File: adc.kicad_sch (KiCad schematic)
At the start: 0 parts

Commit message: Added awags and dac sheet.
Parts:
- added C47, C48: C0402_10uF_6.3V, Capacitor_SMD:C_0402_1005Metric, symbol Jojos_Lib:C0402_10uF_6.3V
- added C50, C53, C56, C59, C62: C0402_1uF_6.3V, Capacitor_SMD:C_0402_1005Metric, symbol Jojos_Lib:C0402_1uF_6.3V
- added C51, C54, C57, C60, C63: C0402_100nF_50V, Capacitor_SMD:C_0402_1005Metric, symbol Jojos_Lib:C0402_100nF_50V
- added U10, U13: 74HCT1G125GW, Package_TO_SOT_SMD:SOT-353_SC-70-5, symbol Jojos_Lib:74HCT1G125GW
- added U9: ADS8584S, Package_QFP:LQFP-64_10x10mm_P0.5mm, symbol Jojos_Lib:ADS8584S
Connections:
- new net 3.3V: C62.1, C63.1, U9.34 (REFSEL), U9.6 (nPAR/SER/BYTE_SEL), U9.7 (nSTBY)
- new net 5V: C50.1, C51.1, C53.1, C54.1, C56.1, C57.1, C59.1, C60.1
- new net BUSY: U9.14 (BUSY)
- new net CONV: U9.10 (CONVSTB), U9.9 (CONVSTA)
- new net FIRST3.3: U9.15 (FRSTDATA)
- new net GND: C50.2, C51.2, C53.2, C54.2, C56.2, C57.2, C59.2, C60.2, C62.2, C63.2, U9.33 (DB15/BYTE_SEL), U9.53 (AGND_passive), U9.54 (AGND_passive), U9.55 (AGND_passive), U9.56 (AGND_passive), U9.61 (AGND_passive), U9.62 (AGND_passive), U9.63 (AGND_passive), U9.64 (AGND_passive), U9.8 (RANGE)
- new net OS0: U9.3 (OS0)
- new net OS1: U9.4 (OS1)
- new net OS2: U9.5 (OS2)
- new net OUT0_M: U9.50 (AIN_1GND)
- new net OUT0_P: U9.49 (AIN_1P)
- new net OUT1_M: U9.52 (AIN_2GND)
- new net OUT1_P: U9.51 (AIN_2P)
- new net OUT2_M: U9.58 (AIN_3GND)
- new net OUT2_P: U9.57 (AIN_3P)
- new net OUT3_M: U9.60 (AIN_4GND)
- new net OUT3_P: U9.59 (AIN_4P)
- new net RST: U9.11 (RESET)
- new net SCLK: U9.12 (nRD/SCLK)
- new net nCS: U9.13 (nCS)
- no-connect marks 0 -> 13

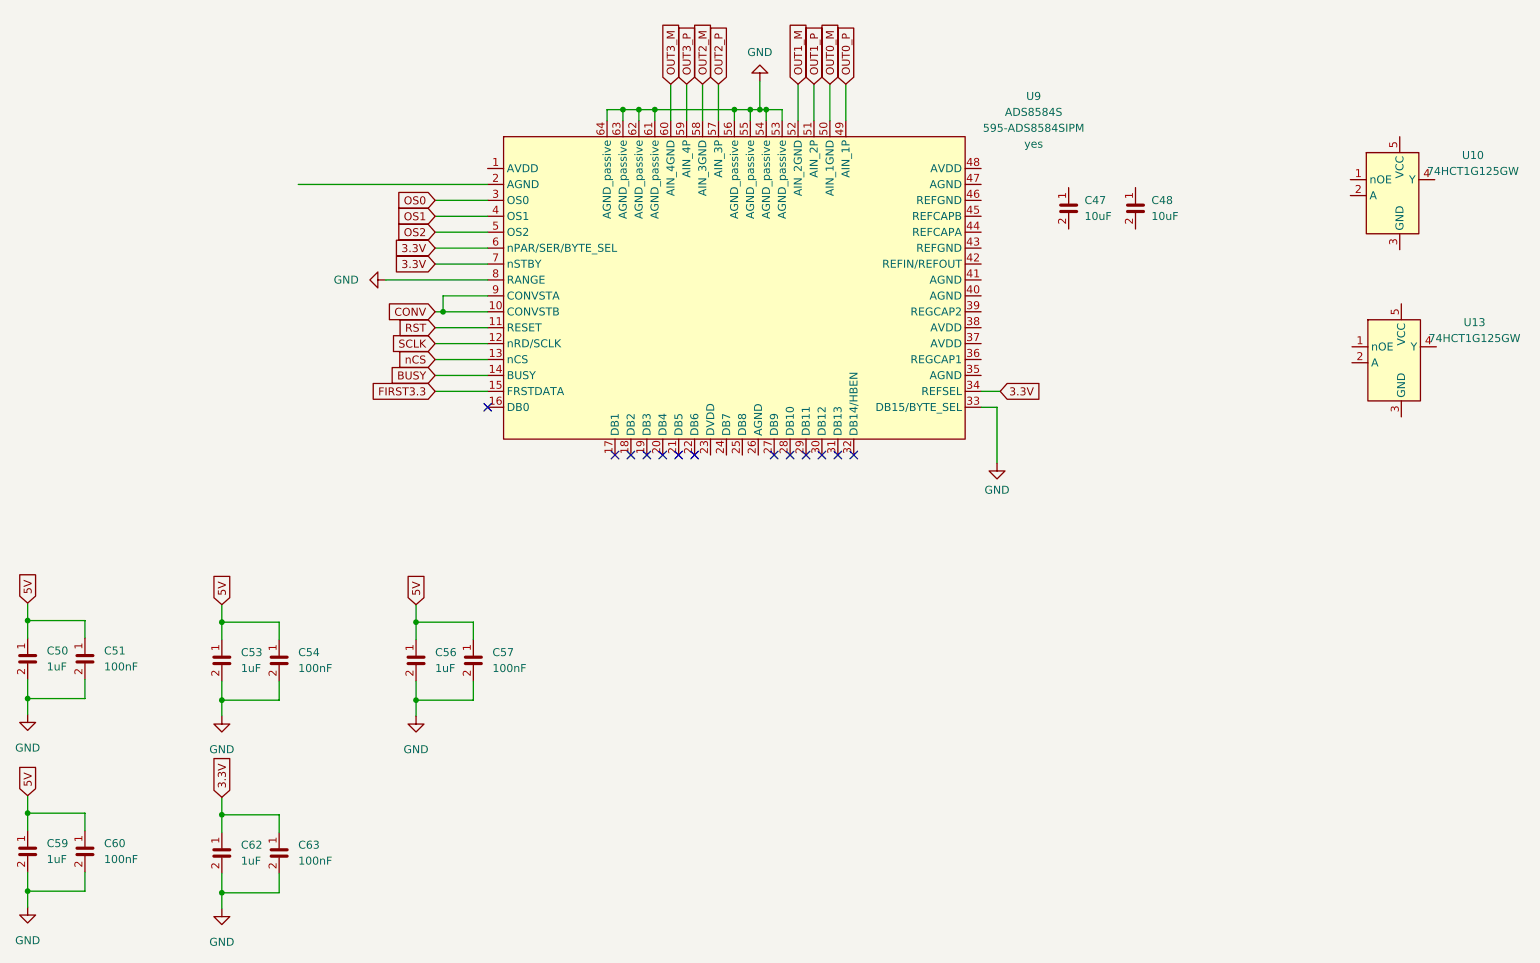
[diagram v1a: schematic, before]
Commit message: Added DAC circuit.
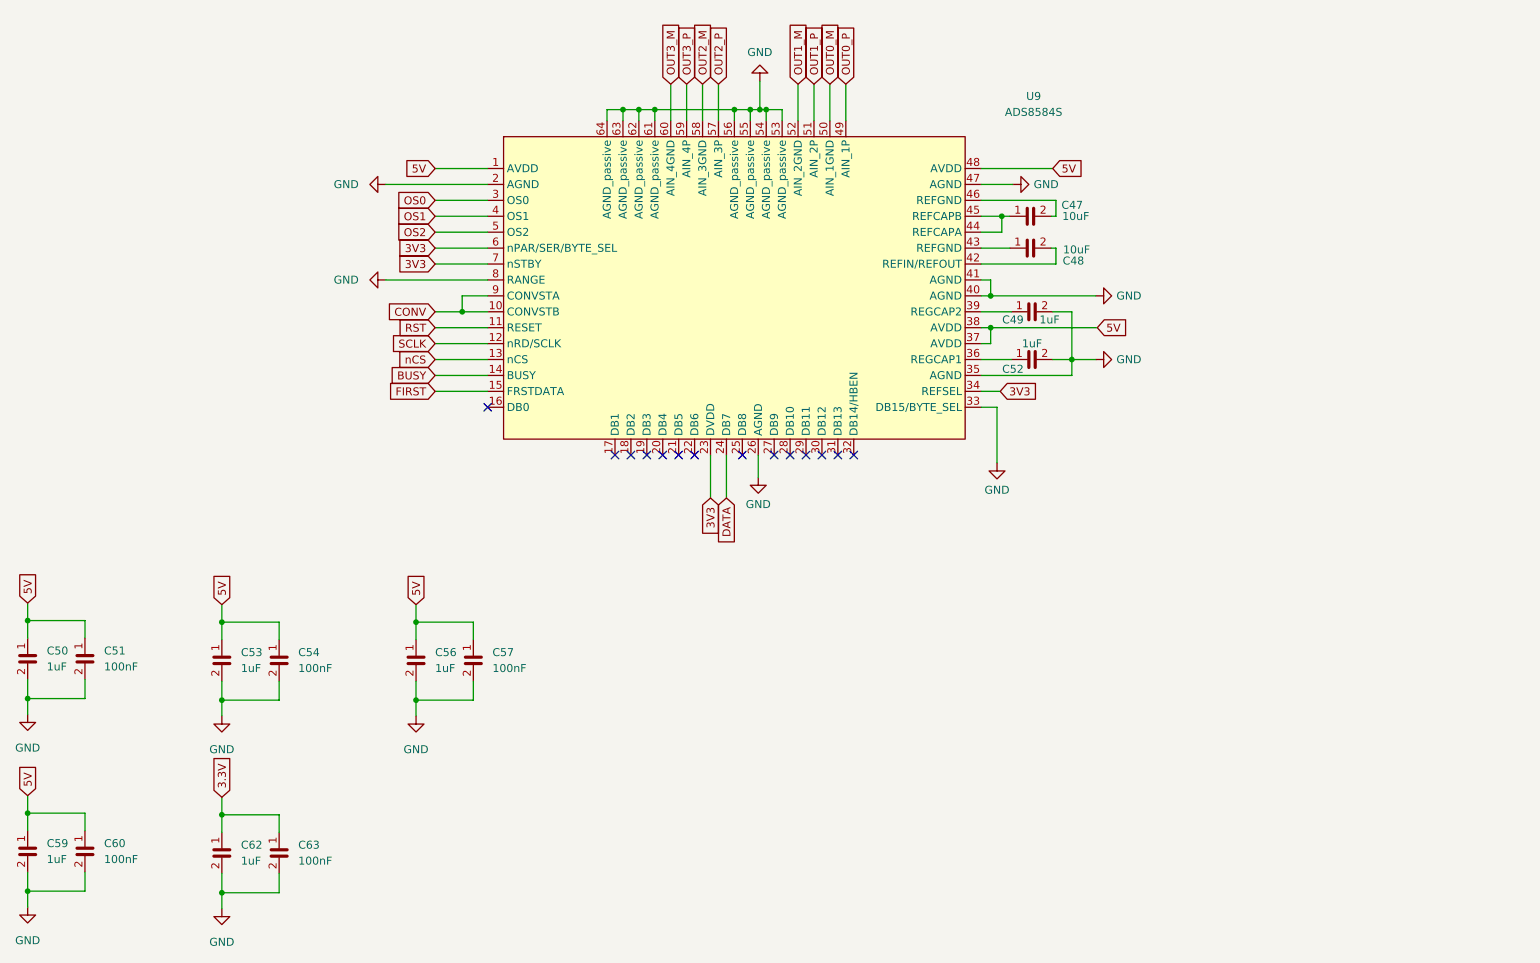
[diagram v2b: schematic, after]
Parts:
- removed U10, U13: 74HCT1G125GW, Package_TO_SOT_SMD:SOT-353_SC-70-5, symbol Jojos_Lib:74HCT1G125GW
- added C49, C52: C0402_1uF_6.3V, Capacitor_SMD:C_0402_1005Metric, symbol Jojos_Lib:C0402_1uF_6.3V
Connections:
- net 3.3V: no longer U9.34 (REFSEL), U9.6 (nPAR/SER/BYTE_SEL), U9.7 (nSTBY)
- net 5V: now also U9.1 (AVDD), U9.37 (AVDD), U9.38 (AVDD), U9.48 (AVDD)
- net GND: now also U9.2 (AGND), U9.26 (AGND), U9.35 (AGND), U9.40 (AGND), U9.41 (AGND), U9.47 (AGND), C49.2, C52.2
- net 3V3: now reaches U9.23 (DVDD)
- net 3V3: now also U9.34 (REFSEL), U9.6 (nPAR/SER/BYTE_SEL), U9.7 (nSTBY)
- net DATA: now reaches U9.24 (DB7)
- net at U9.36 (REGCAP1): now also C52.1
- net at U9.39 (REGCAP2): now also C49.1
- net at U9.42 (REFIN/REFOUT): now also C48.2
- net at U9.43 (REFGND): now also C48.1
- net at U9.44 (REFCAPA): now also C47.1, U9.45 (REFCAPB)
- net at U9.46 (REFGND): now also C47.2
- net FIRST3.3 renamed FIRST
- no-connect marks 13 -> 14
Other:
- moved on the sheet: C47, C48

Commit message: Changed global to hierarchichal lables, reorganized main sheet to get pins to connector.
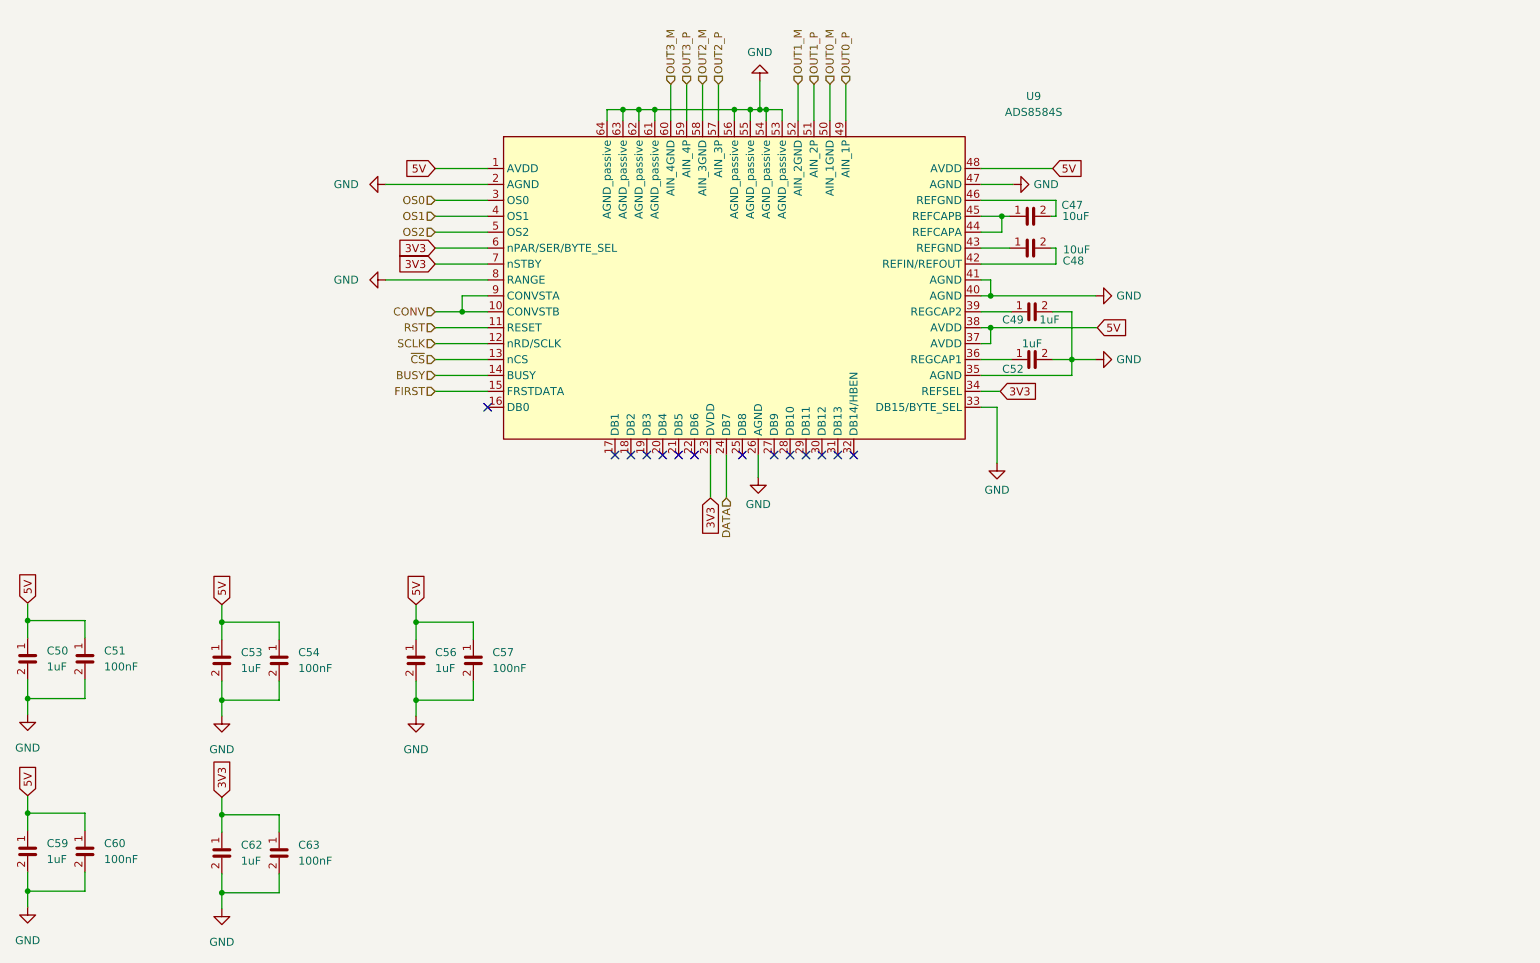
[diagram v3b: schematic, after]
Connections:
- net 3.3V is gone; now on net 3V3: C62.1, C63.1
- net nCS renamed ~{CS}
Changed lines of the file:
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@@
-    )
-  )
-  (global_label "OS0" (shape input) (at 94.488 76.962 180) (fields_autoplaced)
-    (effects (font (size 1.27 1.27)) (justify right))
-    (property "Intersheetrefs" "${INTERSHEET_REFS}" (at 87.8327 76.962 0)
-      (effects (font (size 1.27 1.27)) (justify right) hide)
-    )
-  )
-  (global_label "OS1" (shape input) (at 94.488 79.502 180) (fields_autoplaced)
-    (effects (font (size 1.27 1.27)) (justify right))
-    (property "Intersheetrefs" "${INTERSHEET_REFS}" (at 87.8327 79.502 0)
-      (effects (font (size 1.27 1.27)) (justify right) hide)
-    )
-  )
-  (global_label "SCLK" (shape input) (at 94.488 99.822 180) (fields_autoplaced)
-    (effects (font (size 1.27 1.27)) (justify right))
-    (property "Intersheetrefs" "${INTERSHEET_REFS}" (at 86.8046 99.822 0)
-      (effects (font (size 1.27 1.27)) (justify right) hide)
-    )
-  )
-  (global_label "OUT3_P" (shape input) (at 134.62 58.42 90) (fields_autoplaced)
-    (effects (font (size 1.27 1.27)) (justify left))
-    (property "Intersheetrefs" "${INTERSHEET_REFS}" (at 134.62 48.4385 90)
-      (effects (font (size 1.27 1.27)) (justify left) hide)
-    )
-  )
-  (global_label "RST" (shape input) (at 94.488 97.282 180) (fields_autoplaced)
-    (effects (font (size 1.27 1.27)) (justify right))
-    (property "Intersheetrefs" "${INTERSHEET_REFS}" (at 88.1351 97.282 0)
-      (effects (font (size 1.27 1.27)) (justify right) hide)
-    )
-  )
-  (global_label "OUT2_M" (shape input) (at 137.16 58.42 90) (fields_autoplaced)
-    (effects (font (size 1.27 1.27)) (justify left))
-    (property "Intersheetrefs" "${INTERSHEET_REFS}" (at 137.16 48.2571 90)
-      (effects (font (size 1.27 1.27)) (justify left) hide)
     )
   )
@@
     )
   )
-  (global_label "BUSY" (shape input) (at 94.488 104.902 180) (fields_autoplaced)
-    (effects (font (size 1.27 1.27)) (justify right))
-    (property "Intersheetrefs" "${INTERSHEET_REFS}" (at 86.6836 104.902 0)
-      (effects (font (size 1.27 1.27)) (justify right) hide)
-    )
-  )
-  (global_label "OUT0_P" (shape input) (at 160.02 58.42 90) (fields_autoplaced)
-    (effects (font (size 1.27 1.27)) (justify left))
-    (property "Intersheetrefs" "${INTERSHEET_REFS}" (at 160.02 48.4385 90)
-      (effects (font (size 1.27 1.27)) (justify left) hide)
-    )
-  )
   (global_label "5V" (shape input) (at 60.452 141.478 90) (fields_autoplaced)
     (effects (font (size 1.27 1.27)) (justify left))
     (property "Intersheetrefs" "${INTERSHEET_REFS}" (at 60.452 136.2741 90)
-      (effects (font (size 1.27 1.27)) (justify left) hide)
-    )
-  )
-  (global_label "OUT2_P" (shape input) (at 139.7 58.42 90) (fields_autoplaced)
-    (effects (font (size 1.27 1.27)) (justify left))
-    (property "Intersheetrefs" "${INTERSHEET_REFS}" (at 139.7 48.4385 90)
-      (effects (font (size 1.27 1.27)) (justify left) hide)
-    )
-  )
-  (global_label "OUT1_P" (shape input) (at 154.94 58.42 90) (fields_autoplaced)
-    (effects (font (size 1.27 1.27)) (justify left))
-    (property "Intersheetrefs" "${INTERSHEET_REFS}" (at 154.94 48.4385 90)
       (effects (font (size 1.27 1.27)) (justify left) hide)
     )
@@
     )
   )
-  (global_label "OUT3_M" (shape input) (at 132.08 58.42 90) (fields_autoplaced)
-    (effects (font (size 1.27 1.27)) (justify left))
-    (property "Intersheetrefs" "${INTERSHEET_REFS}" (at 132.08 48.2571 90)
-      (effects (font (size 1.27 1.27)) (justify left) hide)
-    )
-  )
-  (global_label "nCS" (shape input) (at 94.488 102.362 180) (fields_autoplaced)
-    (effects (font (size 1.27 1.27)) (justify right))
-    (property "Intersheetrefs" "${INTERSHEET_REFS}" (at 87.9537 102.362 0)
-      (effects (font (size 1.27 1.27)) (justify right) hide)
-    )
-  )
   (global_label "5V" (shape input) (at 91.44 141.478 90) (fields_autoplaced)
     (effects (font (size 1.27 1.27)) (justify left))
@@
     )
   )
-  (global_label "OUT0_M" (shape input) (at 157.48 58.42 90) (fields_autoplaced)
+  (global_label "3V3" (shape input) (at 60.452 172.212 90) (fields_autoplaced)
     (effects (font (size 1.27 1.27)) (justify left))
-    (property "Intersheetrefs" "${INTERSHEET_REFS}" (at 157.48 48.2571 90)
+    (property "Intersheetrefs" "${INTERSHEET_REFS}" (at 60.452 165.7986 90)
       (effects (font (size 1.27 1.27)) (justify left) hide)
-    )
-  )
-  (global_label "3.3V" (shape input) (at 60.452 172.212 90) (fields_autoplaced)
-    (effects (font (size 1.27 1.27)) (justify left))
-    (property "Intersheetrefs" "${INTERSHEET_REFS}" (at 60.452 165.1938 90)
-      (effects (font (size 1.27 1.27)) (justify left) hide)
-    )
-  )
-  (global_label "CONV" (shape input) (at 94.488 94.742 180) (fields_autoplaced)
-    (effects (font (size 1.27 1.27)) (justify right))
-    (property "Intersheetrefs" "${INTERSHEET_REFS}" (at 86.5626 94.742 0)
-      (effects (font (size 1.27 1.27)) (justify right) hide)
     )
   )
@@
     )
   )
-  (global_label "FIRST" (shape input) (at 94.488 107.442 180) (fields_autoplaced)
-    (effects (font (size 1.27 1.27)) (justify right))
-    (property "Intersheetrefs" "${INTERSHEET_REFS}" (at 86.4417 107.442 0)
-      (effects (font (size 1.27 1.27)) (justify right) hide)
-    )
-  )
   (global_label "5V" (shape input) (at 193.04 71.882 0) (fields_autoplaced)
     (effects (font (size 1.27 1.27)) (justify left))
@@
     )
   )
-  (global_label "OS2" (shape input) (at 94.488 82.042 180) (fields_autoplaced)
+  (hierarchical_label "OUT3_M" (shape input) (at 132.08 58.42 90) (fields_autoplaced)
+    (effects (font (size 1.27 1.27)) (justify left))
+  )
+  (hierarchical_label "RST" (shape input) (at 94.488 97.282 180) (fields_autoplaced)
     (effects (font (size 1.27 1.27)) (justify right))
-    (property "Intersheetrefs" "${INTERSHEET_REFS}" (at 87.8327 82.042 0)
-      (effects (font (size 1.27 1.27)) (justify right) hide)
-    )
   )
-  (global_label "OUT1_M" (shape input) (at 152.4 58.42 90) (fields_autoplaced)
+  (hierarchical_label "OUT0_M" (shape input) (at 157.48 58.42 90) (fields_autoplaced)
     (effects (font (size 1.27 1.27)) (justify left))
-    (property "Intersheetrefs" "${INTERSHEET_REFS}" (at 152.4 48.2571 90)
-      (effects (font (size 1.27 1.27)) (justify left) hide)
-    )
   )
-  (global_label "DATA" (shape input) (at 140.97 124.46 270) (fields_autoplaced)
+  (hierarchical_label "OUT2_P" (shape input) (at 139.7 58.42 90) (fields_autoplaced)
+    (effects (font (size 1.27 1.27)) (justify left))
+  )
+  (hierarchical_label "OS0" (shape input) (at 94.488 76.962 180) (fields_autoplaced)
     (effects (font (size 1.27 1.27)) (justify right))
-    (property "Intersheetrefs" "${INTERSHEET_REFS}" (at 140.97 131.7806 90)
-      (effects (font (size 1.27 1.27)) (justify right) hide)
-    )
+  )
+  (hierarchical_label "FIRST" (shape input) (at 94.488 107.442 180) (fields_autoplaced)
+    (effects (font (size 1.27 1.27)) (justify right))
+  )
+  (hierarchical_label "OUT1_M" (shape input) (at 152.4 58.42 90) (fields_autoplaced)
+    (effects (font (size 1.27 1.27)) (justify left))
+  )
+  (hierarchical_label "DATA" (shape input) (at 140.97 124.46 270) (fields_autoplaced)
+    (effects (font (size 1.27 1.27)) (justify right))
+  )
+  (hierarchical_label "CONV" (shape input) (at 94.488 94.742 180) (fields_autoplaced)
+    (effects (font (size 1.27 1.27)) (justify right))
+  )
+  (hierarchical_label "~{CS}" (shape input) (at 94.488 102.362 180) (fields_autoplaced)
+    (effects (font (size 1.27 1.27)) (justify right))
+  )
+  (hierarchical_label "OUT3_P" (shape input) (at 134.62 58.42 90) (fields_autoplaced)
+    (effects (font (size 1.27 1.27)) (justify left))
+  )
+  (hierarchical_label "OUT1_P" (shape input) (at 154.94 58.42 90) (fields_autoplaced)
+    (effects (font (size 1.27 1.27)) (justify left))
+  )
+  (hierarchical_label "BUSY" (shape input) (at 94.488 104.902 180) (fields_autoplaced)
+    (effects (font (size 1.27 1.27)) (justify right))
+  )
+  (hierarchical_label "OUT2_M" (shape input) (at 137.16 58.42 90) (fields_autoplaced)
+    (effects (font (size 1.27 1.27)) (justify left))
+  )
+  (hierarchical_label "OS2" (shape input) (at 94.488 82.042 180) (fields_autoplaced)
+    (effects (font (size 1.27 1.27)) (justify right))
+  )
+  (hierarchical_label "OUT0_P" (shape input) (at 160.02 58.42 90) (fields_autoplaced)
+    (effects (font (size 1.27 1.27)) (justify left))
+  )
+  (hierarchical_label "SCLK" (shape input) (at 94.488 99.822 180) (fields_autoplaced)
+    (effects (font (size 1.27 1.27)) (justify right))
+  )
+  (hierarchical_label "OS1" (shape input) (at 94.488 79.502 180) (fields_autoplaced)
+    (effects (font (size 1.27 1.27)) (justify right))
   )
   (symbol (lib_id "Jojos_Lib:ADS8584S") (at 142.24 90.932 0) (unit 1)
